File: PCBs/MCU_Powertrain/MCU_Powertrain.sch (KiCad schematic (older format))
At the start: 53 parts, among them J1 PHASE_A, J2 PHASE_B, J3 PHASE_C, J4 Big Conn, J5 Pogo Conn, J6 Conn CAN, J7 PWRIN, U2 SN65HVD232, U3 MCP2515, U4 LMR16006XDDC, Y1 20MHz

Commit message: Routing
- Routed most of DRV and TI chips
- FETs are done
- Added board outline
- Added power and ground planes
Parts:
- TP1, TP10, TP11, TP12, TP13, TP14, TP15, TP16, TP17, TP18, TP19, TP2, TP20, TP21, TP3, TP4, TP5, TP6, TP7, TP8, TP9: footprint Testpoints:TestPoint_Loop_D1.80mm_Drill1.0mm_Beaded -> MCU_Powertrain:TestPoint_Loop_D1.80mm_Drill1.0mm_Beaded
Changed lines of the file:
@@
 F 0 "TP6" H 10308 3918 50  0000 L CNN
 F 1 "TestPoint" H 10308 3827 50  0000 L CNN
-F 2 "Testpoints:TestPoint_Loop_D1.80mm_Drill1.0mm_Beaded" H 10450 3800 50  0001 C CNN
+F 2 "MCU_Powertrain:TestPoint_Loop_D1.80mm_Drill1.0mm_Beaded" H 10450 3800 50  0001 C CNN
 F 3 "~" H 10450 3800 50  0001 C CNN
 F 4 "36-5119-ND" H 10250 3800 50  0001 C CNN "Digikey"
@@
 F 0 "TP18" H 4658 5143 50  0000 L CNN
 F 1 "TestPoint" H 4658 5052 50  0000 L CNN
-F 2 "Testpoints:TestPoint_Loop_D1.80mm_Drill1.0mm_Beaded" H 4800 5025 50  0001 C CNN
+F 2 "MCU_Powertrain:TestPoint_Loop_D1.80mm_Drill1.0mm_Beaded" H 4800 5025 50  0001 C CNN
 F 3 "~" H 4800 5025 50  0001 C CNN
 F 4 "36-5000-ND" H 4600 5025 50  0001 C CNN "Digikey"
@@
 F 0 "TP20" H 2308 5493 50  0000 L CNN
 F 1 "TestPoint" H 2308 5402 50  0000 L CNN
-F 2 "Testpoints:TestPoint_Loop_D1.80mm_Drill1.0mm_Beaded" H 2450 5375 50  0001 C CNN
+F 2 "MCU_Powertrain:TestPoint_Loop_D1.80mm_Drill1.0mm_Beaded" H 2450 5375 50  0001 C CNN
 F 3 "~" H 2450 5375 50  0001 C CNN
 F 4 "36-5000-ND" H 2250 5375 50  0001 C CNN "Digikey"
@@
 F 0 "TP12" V 1275 4400 50  0000 L CNN
 F 1 "TestPoint" V 1350 4550 50  0000 L CNN
-F 2 "Testpoints:TestPoint_Loop_D1.80mm_Drill1.0mm_Beaded" H 1550 4375 50  0001 C CNN
+F 2 "MCU_Powertrain:TestPoint_Loop_D1.80mm_Drill1.0mm_Beaded" H 1550 4375 50  0001 C CNN
 F 3 "~" H 1550 4375 50  0001 C CNN
 F 4 "36-5119-ND" V 1350 4375 50  0001 C CNN "Digikey"
@@
 F 0 "TP1" V 10425 2825 50  0000 L CNN
 F 1 "TestPoint" V 10500 2975 50  0000 L CNN
-F 2 "Testpoints:TestPoint_Loop_D1.80mm_Drill1.0mm_Beaded" H 10700 2800 50  0001 C CNN
+F 2 "MCU_Powertrain:TestPoint_Loop_D1.80mm_Drill1.0mm_Beaded" H 10700 2800 50  0001 C CNN
 F 3 "~" H 10700 2800 50  0001 C CNN
 F 4 "36-5117-ND" V 10500 2800 50  0001 C CNN "Digikey"
@@
 F 0 "TP2" V 10425 2975 50  0000 L CNN
 F 1 "TestPoint" V 10500 3125 50  0000 L CNN
-F 2 "Testpoints:TestPoint_Loop_D1.80mm_Drill1.0mm_Beaded" H 10700 2950 50  0001 C CNN
+F 2 "MCU_Powertrain:TestPoint_Loop_D1.80mm_Drill1.0mm_Beaded" H 10700 2950 50  0001 C CNN
 F 3 "~" H 10700 2950 50  0001 C CNN
 F 4 "36-5117-ND" V 10500 2950 50  0001 C CNN "Digikey"
@@
 F 0 "TP3" V 10425 3125 50  0000 L CNN
 F 1 "TestPoint" V 10500 3275 50  0000 L CNN
-F 2 "Testpoints:TestPoint_Loop_D1.80mm_Drill1.0mm_Beaded" H 10700 3100 50  0001 C CNN
+F 2 "MCU_Powertrain:TestPoint_Loop_D1.80mm_Drill1.0mm_Beaded" H 10700 3100 50  0001 C CNN
 F 3 "~" H 10700 3100 50  0001 C CNN
 F 4 "36-5117-ND" V 10500 3100 50  0001 C CNN "Digikey"
@@
 F 0 "TP4" V 10425 3325 50  0000 L CNN
 F 1 "TestPoint" V 10500 3475 50  0000 L CNN
-F 2 "Testpoints:TestPoint_Loop_D1.80mm_Drill1.0mm_Beaded" H 10700 3300 50  0001 C CNN
+F 2 "MCU_Powertrain:TestPoint_Loop_D1.80mm_Drill1.0mm_Beaded" H 10700 3300 50  0001 C CNN
 F 3 "~" H 10700 3300 50  0001 C CNN
 F 4 "36-5001-ND" V 10500 3300 50  0001 C CNN "Digikey"
@@
 F 0 "TP19" V 7100 5250 50  0000 L CNN
 F 1 "TestPoint" V 7175 5400 50  0000 L CNN
-F 2 "Testpoints:TestPoint_Loop_D1.80mm_Drill1.0mm_Beaded" H 7375 5225 50  0001 C CNN
+F 2 "MCU_Powertrain:TestPoint_Loop_D1.80mm_Drill1.0mm_Beaded" H 7375 5225 50  0001 C CNN
 F 3 "~" H 7375 5225 50  0001 C CNN
 F 4 "36-5001-ND" V 7175 5225 50  0001 C CNN "Digikey"
@@
 F 0 "TP21" V 7100 5425 50  0000 L CNN
 F 1 "TestPoint" V 7175 5575 50  0000 L CNN
-F 2 "Testpoints:TestPoint_Loop_D1.80mm_Drill1.0mm_Beaded" H 7375 5400 50  0001 C CNN
+F 2 "MCU_Powertrain:TestPoint_Loop_D1.80mm_Drill1.0mm_Beaded" H 7375 5400 50  0001 C CNN
 F 3 "~" H 7375 5400 50  0001 C CNN
 F 4 "36-5001-ND" V 7175 5400 50  0001 C CNN "Digikey"
@@
 F 0 "TP10" H 10192 4126 50  0000 R CNN
 F 1 "TestPoint" H 10192 4217 50  0000 R CNN
-F 2 "Testpoints:TestPoint_Loop_D1.80mm_Drill1.0mm_Beaded" H 10450 4100 50  0001 C CNN
+F 2 "MCU_Powertrain:TestPoint_Loop_D1.80mm_Drill1.0mm_Beaded" H 10450 4100 50  0001 C CNN
 F 3 "~" H 10450 4100 50  0001 C CNN
 F 4 "36-5119-ND" H 10250 4100 50  0001 C CNN "Digikey"
@@
 F 0 "TP5" H 8983 3818 50  0000 L CNN
 F 1 "TestPoint" H 8983 3727 50  0000 L CNN
-F 2 "Testpoints:TestPoint_Loop_D1.80mm_Drill1.0mm_Beaded" H 9125 3700 50  0001 C CNN
+F 2 "MCU_Powertrain:TestPoint_Loop_D1.80mm_Drill1.0mm_Beaded" H 9125 3700 50  0001 C CNN
 F 3 "~" H 9125 3700 50  0001 C CNN
 F 4 "36-5119-ND" H 8925 3700 50  0001 C CNN "Digikey"
@@
 F 0 "TP8" H 8867 4051 50  0000 R CNN
 F 1 "TestPoint" H 8867 4142 50  0000 R CNN
-F 2 "Testpoints:TestPoint_Loop_D1.80mm_Drill1.0mm_Beaded" H 9125 4025 50  0001 C CNN
+F 2 "MCU_Powertrain:TestPoint_Loop_D1.80mm_Drill1.0mm_Beaded" H 9125 4025 50  0001 C CNN
 F 3 "~" H 9125 4025 50  0001 C CNN
 F 4 "36-5119-ND" H 8925 4025 50  0001 C CNN "Digikey"
@@
 F 0 "TP14" V 1275 4575 50  0000 L CNN
 F 1 "TestPoint" V 1350 4725 50  0000 L CNN
-F 2 "Testpoints:TestPoint_Loop_D1.80mm_Drill1.0mm_Beaded" H 1550 4550 50  0001 C CNN
+F 2 "MCU_Powertrain:TestPoint_Loop_D1.80mm_Drill1.0mm_Beaded" H 1550 4550 50  0001 C CNN
 F 3 "~" H 1550 4550 50  0001 C CNN
 F 4 "36-5119-ND" V 1350 4550 50  0001 C CNN "Digikey"
@@
 F 0 "TP17" V 2350 4900 50  0000 L CNN
 F 1 "TestPoint" V 2425 5050 50  0000 L CNN
-F 2 "Testpoints:TestPoint_Loop_D1.80mm_Drill1.0mm_Beaded" H 2625 4875 50  0001 C CNN
+F 2 "MCU_Powertrain:TestPoint_Loop_D1.80mm_Drill1.0mm_Beaded" H 2625 4875 50  0001 C CNN
 F 3 "~" H 2625 4875 50  0001 C CNN
 F 4 "36-5001-ND" V 2425 4875 50  0001 C CNN "Digikey"
@@
 F 0 "TP16" V 2350 4750 50  0000 L CNN
 F 1 "TestPoint" V 2425 4900 50  0000 L CNN
-F 2 "Testpoints:TestPoint_Loop_D1.80mm_Drill1.0mm_Beaded" H 2625 4725 50  0001 C CNN
+F 2 "MCU_Powertrain:TestPoint_Loop_D1.80mm_Drill1.0mm_Beaded" H 2625 4725 50  0001 C CNN
 F 3 "~" H 2625 4725 50  0001 C CNN
 F 4 "36-5001-ND" V 2425 4725 50  0001 C CNN "Digikey"
@@
 F 0 "TP7" V 2350 3975 50  0000 L CNN
 F 1 "TestPoint" V 2425 4125 50  0000 L CNN
-F 2 "Testpoints:TestPoint_Loop_D1.80mm_Drill1.0mm_Beaded" H 2625 3950 50  0001 C CNN
+F 2 "MCU_Powertrain:TestPoint_Loop_D1.80mm_Drill1.0mm_Beaded" H 2625 3950 50  0001 C CNN
 F 3 "~" H 2625 3950 50  0001 C CNN
 F 4 "36-5119-ND" V 2425 3950 50  0001 C CNN "Digikey"
@@
 F 0 "TP9" V 2350 4125 50  0000 L CNN
 F 1 "TestPoint" V 2425 4275 50  0000 L CNN
-F 2 "Testpoints:TestPoint_Loop_D1.80mm_Drill1.0mm_Beaded" H 2625 4100 50  0001 C CNN
+F 2 "MCU_Powertrain:TestPoint_Loop_D1.80mm_Drill1.0mm_Beaded" H 2625 4100 50  0001 C CNN
 F 3 "~" H 2625 4100 50  0001 C CNN
 F 4 "36-5119-ND" V 2425 4100 50  0001 C CNN "Digikey"
@@
 F 0 "TP11" V 2350 4275 50  0000 L CNN
 F 1 "TestPoint" V 2425 4425 50  0000 L CNN
-F 2 "Testpoints:TestPoint_Loop_D1.80mm_Drill1.0mm_Beaded" H 2625 4250 50  0001 C CNN
+F 2 "MCU_Powertrain:TestPoint_Loop_D1.80mm_Drill1.0mm_Beaded" H 2625 4250 50  0001 C CNN
 F 3 "~" H 2625 4250 50  0001 C CNN
 F 4 "36-5119-ND" V 2425 4250 50  0001 C CNN "Digikey"
@@
 F 0 "TP13" V 2350 4425 50  0000 L CNN
 F 1 "TestPoint" V 2425 4575 50  0000 L CNN
-F 2 "Testpoints:TestPoint_Loop_D1.80mm_Drill1.0mm_Beaded" H 2625 4400 50  0001 C CNN
+F 2 "MCU_Powertrain:TestPoint_Loop_D1.80mm_Drill1.0mm_Beaded" H 2625 4400 50  0001 C CNN
 F 3 "~" H 2625 4400 50  0001 C CNN
 F 4 "36-5119-ND" V 2425 4400 50  0001 C CNN "Digikey"
@@
 F 0 "TP15" V 2350 4575 50  0000 L CNN
 F 1 "TestPoint" V 2425 4725 50  0000 L CNN
-F 2 "Testpoints:TestPoint_Loop_D1.80mm_Drill1.0mm_Beaded" H 2625 4550 50  0001 C CNN
+F 2 "MCU_Powertrain:TestPoint_Loop_D1.80mm_Drill1.0mm_Beaded" H 2625 4550 50  0001 C CNN
 F 3 "~" H 2625 4550 50  0001 C CNN
 F 4 "36-5119-ND" V 2425 4550 50  0001 C CNN "Digikey"

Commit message: Initial Routing Complete
- Connected all nets, no DRC errors
- Still need to investigate the CAN logic level and add in a termination resistor
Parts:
- Y1: symbol Device:Crystal_Small -> Device:Crystal_GND24
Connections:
- wire segments 216 -> 220
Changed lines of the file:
@@
 	6475 4275 7650 4275
 NoConn ~ 7650 4775
-$Comp
-L Device:Crystal_Small Y1
-U 1 1 5E45594D
-P 7175 4650
-F 0 "Y1" V 7221 4562 50  0000 R CNN
-F 1 "20MHz" V 7130 4562 50  0000 R CNN
-F 2 "Crystals:Crystal_SMD_SeikoEpson_TSX3225-4pin_3.2x2.5mm" H 7175 4650 50  0001 C CNN
-F 3 "~" H 7175 4650 50  0001 C CNN
-F 4 "SER4249CT-ND" V 7175 4650 50  0001 C CNN "Digikey"
-	1    7175 4650
-	0    -1   -1   0
-$EndComp
 Wire Wire Line
 	7650 4575 7600 4575
@@
 	7600 4450 7175 4450
 Wire Wire Line
-	7175 4450 7175 4550
+	7175 4450 7175 4500
 Wire Wire Line
 	7650 4675 7600 4675
@@
 Wire Wire Line
 	7600 4825 7175 4825
-Wire Wire Line
-	7175 4825 7175 4750
 $Comp
 L Device:C_Small C21
 U 1 1 5E462988
 P 6950 4450
-F 0 "C21" V 6825 4450 50  0000 C CNN
-F 1 "15pF" V 7075 4450 50  0000 C CNN
+F 0 "C21" V 6900 4350 50  0000 C CNN
+F 1 "15pF" V 7000 4325 50  0000 C CNN
 F 2 "Capacitors_SMD:C_0603" H 6950 4450 50  0001 C CNN
 F 3 "~" H 6950 4450 50  0001 C CNN
@@
 U 1 1 5E463EDB
 P 6950 4825
-F 0 "C22" V 6825 4825 50  0000 C CNN
-F 1 "15pF" V 7075 4825 50  0000 C CNN
+F 0 "C22" V 6900 4700 50  0000 C CNN
+F 1 "15pF" V 7000 4700 50  0000 C CNN
 F 2 "Capacitors_SMD:C_0603" H 6950 4825 50  0001 C CNN
 F 3 "~" H 6950 4825 50  0001 C CNN
@@
 	1    0    0    -1
 $EndComp
+Wire Wire Line
+	7175 4825 7175 4800
+$Comp
+L Device:Crystal_GND24 Y1
+U 1 1 5E45594D
+P 7175 4650
+F 0 "Y1" V 7325 4600 50  0000 R CNN
+F 1 "20MHz" V 6925 4750 50  0000 R CNN
+F 2 "Crystals:Crystal_SMD_SeikoEpson_TSX3225-4pin_3.2x2.5mm" H 7175 4650 50  0001 C CNN
+F 3 "~" H 7175 4650 50  0001 C CNN
+F 4 "SER4249CT-ND" V 7175 4650 50  0001 C CNN "Digikey"
+	1    7175 4650
+	0    -1   -1   0
+$EndComp
+Wire Wire Line
+	7375 4650 7425 4650
+Wire Wire Line
+	7425 4650 7425 4700
+Wire Wire Line
+	6975 4650 7375 4650
+Connection ~ 7375 4650
+Wire Wire Line
+	7375 4650 7425 4650
+$Comp
+L power:GND #PWR?
+U 1 1 5E49D106
+P 7425 4700
+AR Path="/5E20A2BB/5E49D106" Ref="#PWR?"  Part="1"
+AR Path="/5E49D106" Ref="#PWR?"  Part="1"
+F 0 "#PWR?" H 7425 4450 50  0001 C CNN
+F 1 "GND" H 7500 4700 50  0000 C CNN
+F 2 "" H 7425 4700 50  0001 C CNN
+F 3 "" H 7425 4700 50  0001 C CNN
+	1    7425 4700
+	1    0    0    -1
+$EndComp

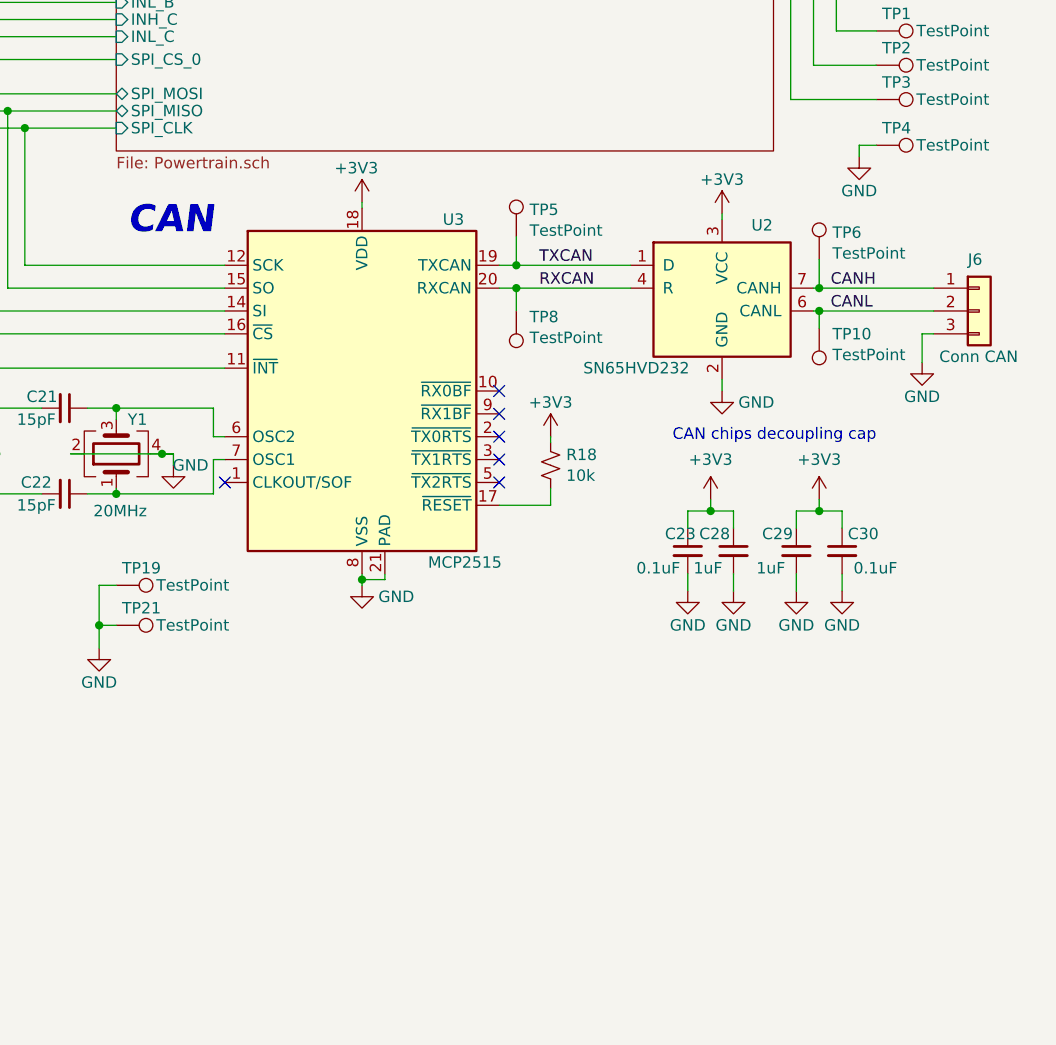
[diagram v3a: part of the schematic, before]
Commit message: Countour and CAN
- Shrunk board outline
- Swapped out CAN tranciever
- Added 5V LDO for CAN outputs, CAN now 5V compatible
- Checked over layout
- Everything finished except silkscreen
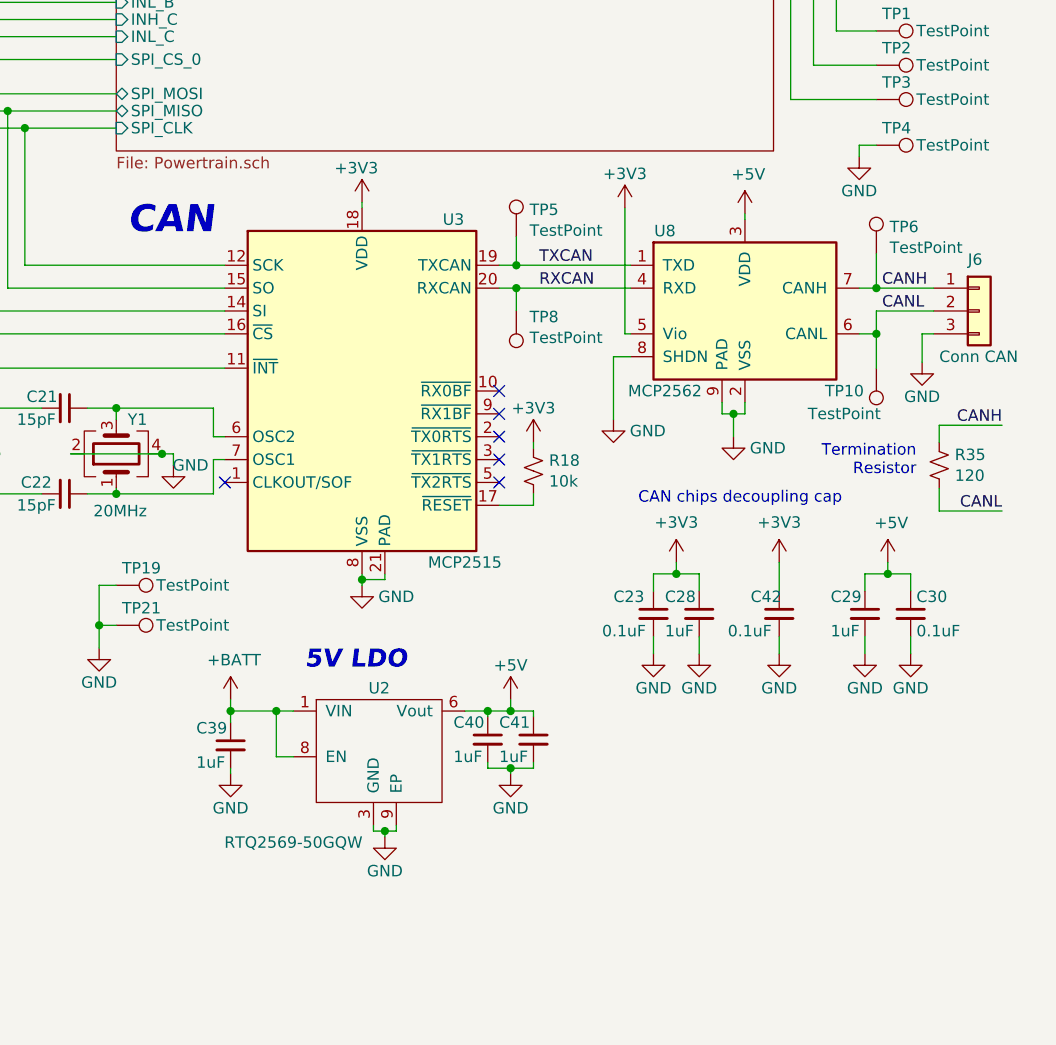
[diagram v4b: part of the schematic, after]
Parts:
- removed U2: SN65HVD232, Housings_SOIC:SOIC-8_3.9x4.9mm_Pitch1.27mm, symbol Interface_CAN_LIN:SN65HVD232
- added C39, C40, C41: 1uF, Capacitors_SMD:C_0805, symbol Device:C_Small
- added C42: 0.1uF, Capacitors_SMD:C_0603, symbol Device:C_Small
- added R35: 120, Resistors_SMD:R_0805, symbol Device:R_Small_US
- added U2: RTQ2569-50GQW, Housings_DFN_QFN:DFN-8-1EP_3x3mm_Pitch0.65mm, symbol MCU_Powertrain:RTQ2569-50GQW
- added U8: MCP2562, Housings_DFN_QFN:DFN-8-1EP_3x3mm_Pitch0.65mm, symbol Interface_CAN_LIN:MCP2562-E-MF
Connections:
- net labels added: +5V
- wire segments 220 -> 257
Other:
- note added: "5V LDO"
- note added: "Termination\nResistor"
- moved on the sheet: C23, C28, C29, C30, R18, TP10, TP6

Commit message: BOM Exporting
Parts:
- C39: value 1uF -> 1.01uF; Voltage (none) -> 35V
- R19: Digikey A129743CT-ND -> RHM330DCT-ND
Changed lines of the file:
@@
 F 2 "Resistors_SMD:R_0603" V 5365 5890 50  0001 C CNN
 F 3 "~" H 5325 5900 50  0001 C CNN
-F 4 "A129743CT-ND" H 5325 5900 50  0001 C CNN "Digikey"
+F 4 "RHM330DCT-ND" H 5325 5900 50  0001 C CNN "Digikey"
 	1    5325 5900
 	1    0    0    -1
@@
 AR Path="/5E20A2BB/5E6BC1B4" Ref="C?"  Part="1"
 AR Path="/5E6BC1B4" Ref="C42"  Part="1"
-F 0 "C42" H 9950 5425 50  0000 L CNN
+F 0 "C42" H 9900 5425 50  0000 L CNN
 F 1 "0.1uF" H 9850 5275 50  0000 L CNN
 F 2 "Capacitors_SMD:C_0603" H 10075 5350 50  0001 C CNN
@@
 F 3 "" H 8900 5725 50  0001 C CNN
 	1    8900 5725
-	1    0    0    -1
-$EndComp
-$Comp
-L Device:C_Small C?
-U 1 1 5E7B6E45
-P 7675 5925
-AR Path="/5E20A2BB/5E7B6E45" Ref="C?"  Part="1"
-AR Path="/5E7B6E45" Ref="C39"  Part="1"
-F 0 "C39" H 7525 6000 50  0000 L CNN
-F 1 "1uF" H 7525 5850 50  0000 L CNN
-F 2 "Capacitors_SMD:C_0805" H 7675 5925 50  0001 C CNN
-F 3 "" H 7675 5925 50  0001 C CNN
-F 4 "311-1909-1-ND" H 7675 5925 50  0001 C CNN "Digikey"
-	1    7675 5925
 	1    0    0    -1
 $EndComp
@@
 	1    0    0    -1
 $EndComp
+$Comp
+L Device:C_Small C?
+U 1 1 5E7B6E45
+P 7675 5925
+AR Path="/5E20A2BB/5E7B6E45" Ref="C?"  Part="1"
+AR Path="/5E7B6E45" Ref="C39"  Part="1"
+F 0 "C39" H 7500 6000 50  0000 L CNN
+F 1 "1.01uF" H 7400 5850 50  0000 L CNN
+F 2 "Capacitors_SMD:C_0805" H 7675 5925 50  0001 C CNN
+F 3 "" H 7675 5925 50  0001 C CNN
+F 4 "311-1909-1-ND" H 7675 5925 50  0001 C CNN "Digikey"
+F 5 "35V" H 7575 6075 50  0000 C CNN "Voltage"
+	1    7675 5925
+	1    0    0    -1
+$EndComp
